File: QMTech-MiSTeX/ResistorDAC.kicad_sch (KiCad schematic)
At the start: 6 parts

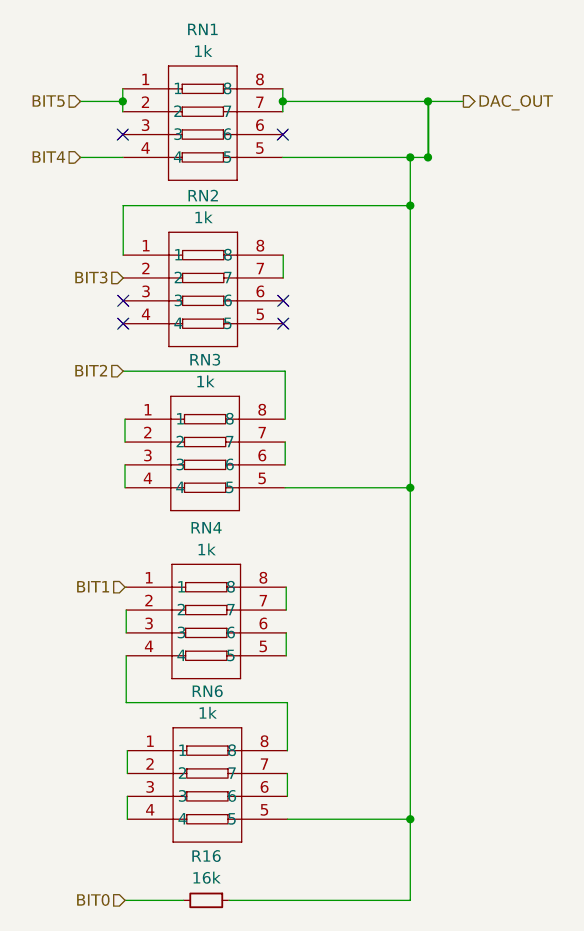
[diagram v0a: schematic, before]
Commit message: apply review notes from somhi, move audio into its own subsheet, add analog audio out
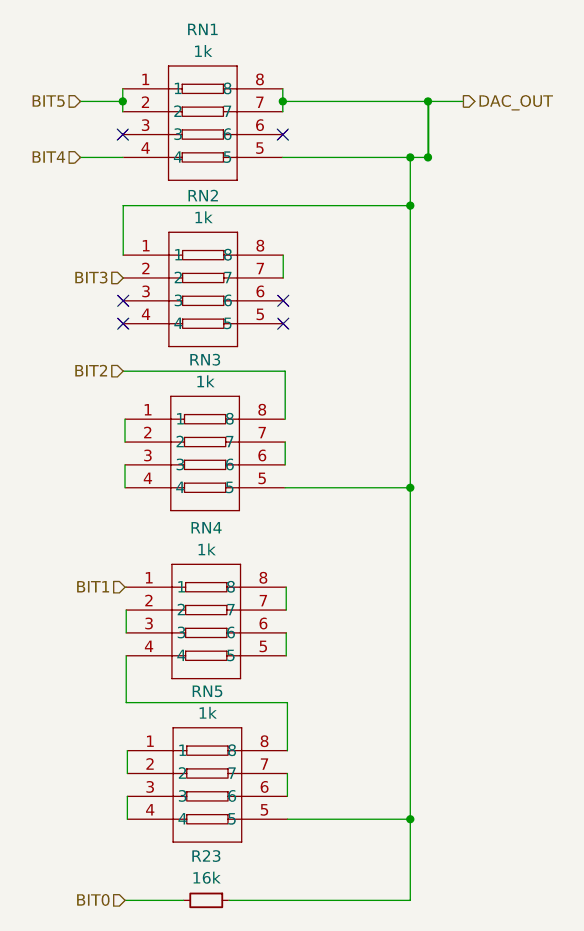
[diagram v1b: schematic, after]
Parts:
- renumbered R16 to R23, RN6 to RN5
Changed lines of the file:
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@@
         )
         (path "/bf95850e-2fcb-4784-a603-f17fc357556b/8c1d97fc-c85e-4afc-840e-7429a199eff3/cbe700d5-28fb-44ad-a669-c9e6c7dd5ddf"
-          (reference "RN1") (unit 1)
+          (reference "RN6") (unit 1)
         )
         (path "/bf95850e-2fcb-4784-a603-f17fc357556b/8c1d97fc-c85e-4afc-840e-7429a199eff3/5343cc42-a3e0-4d70-bd9b-00dc43ec6d46"
-          (reference "RN1") (unit 1)
+          (reference "RN11") (unit 1)
         )
       )
@@
   (symbol (lib_id "jlcpcb-basic-resistor-0603:16k") (at 96.393 134.747 270) (unit 1)
     (in_bom yes) (on_board yes) (dnp no) (fields_autoplaced)
-    (property "Reference" "R16" (at 96.393 129.8661 90)
+    (property "Reference" "R23" (at 96.393 129.8661 90)
       (effects (font (size 1.27 1.27)))
     )
@@
       (project "QMTech-MiSTeX"
         (path "/bf95850e-2fcb-4784-a603-f17fc357556b/8c1d97fc-c85e-4afc-840e-7429a199eff3/0f313b2c-44f6-4c87-90b4-abbb81c512aa"
-          (reference "R16") (unit 1)
+          (reference "R23") (unit 1)
         )
         (path "/bf95850e-2fcb-4784-a603-f17fc357556b/8c1d97fc-c85e-4afc-840e-7429a199eff3/cbe700d5-28fb-44ad-a669-c9e6c7dd5ddf"
-          (reference "R16") (unit 1)
+          (reference "R24") (unit 1)
         )
         (path "/bf95850e-2fcb-4784-a603-f17fc357556b/8c1d97fc-c85e-4afc-840e-7429a199eff3/5343cc42-a3e0-4d70-bd9b-00dc43ec6d46"
-          (reference "R16") (unit 1)
+          (reference "R25") (unit 1)
         )
       )
@@
         )
         (path "/bf95850e-2fcb-4784-a603-f17fc357556b/8c1d97fc-c85e-4afc-840e-7429a199eff3/cbe700d5-28fb-44ad-a669-c9e6c7dd5ddf"
-          (reference "RN2") (unit 1)
+          (reference "RN7") (unit 1)
         )
         (path "/bf95850e-2fcb-4784-a603-f17fc357556b/8c1d97fc-c85e-4afc-840e-7429a199eff3/5343cc42-a3e0-4d70-bd9b-00dc43ec6d46"
-          (reference "RN2") (unit 1)
+          (reference "RN12") (unit 1)
         )
       )
@@
         )
         (path "/bf95850e-2fcb-4784-a603-f17fc357556b/8c1d97fc-c85e-4afc-840e-7429a199eff3/cbe700d5-28fb-44ad-a669-c9e6c7dd5ddf"
-          (reference "RN4") (unit 1)
+          (reference "RN9") (unit 1)
         )
         (path "/bf95850e-2fcb-4784-a603-f17fc357556b/8c1d97fc-c85e-4afc-840e-7429a199eff3/5343cc42-a3e0-4d70-bd9b-00dc43ec6d46"
-          (reference "RN4") (unit 1)
+          (reference "RN14") (unit 1)
         )
       )
@@
   (symbol (lib_id "easyeda2kicad:4D03WGJ0102T5E") (at 96.52 121.92 0) (unit 1)
     (in_bom yes) (on_board yes) (dnp no) (fields_autoplaced)
-    (property "Reference" "RN6" (at 96.52 111.5527 0)
+    (property "Reference" "RN5" (at 96.52 111.5527 0)
       (effects (font (size 1.27 1.27)))
     )
@@
       (project "QMTech-MiSTeX"
         (path "/bf95850e-2fcb-4784-a603-f17fc357556b/8c1d97fc-c85e-4afc-840e-7429a199eff3/0f313b2c-44f6-4c87-90b4-abbb81c512aa"
-          (reference "RN6") (unit 1)
+          (reference "RN5") (unit 1)
         )
         (path "/bf95850e-2fcb-4784-a603-f17fc357556b/8c1d97fc-c85e-4afc-840e-7429a199eff3/cbe700d5-28fb-44ad-a669-c9e6c7dd5ddf"
-          (reference "RN6") (unit 1)
+          (reference "RN10") (unit 1)
         )
         (path "/bf95850e-2fcb-4784-a603-f17fc357556b/8c1d97fc-c85e-4afc-840e-7429a199eff3/5343cc42-a3e0-4d70-bd9b-00dc43ec6d46"
-          (reference "RN6") (unit 1)
+          (reference "RN15") (unit 1)
         )
       )
@@
         )
         (path "/bf95850e-2fcb-4784-a603-f17fc357556b/8c1d97fc-c85e-4afc-840e-7429a199eff3/cbe700d5-28fb-44ad-a669-c9e6c7dd5ddf"
-          (reference "RN3") (unit 1)
+          (reference "RN8") (unit 1)
         )
         (path "/bf95850e-2fcb-4784-a603-f17fc357556b/8c1d97fc-c85e-4afc-840e-7429a199eff3/5343cc42-a3e0-4d70-bd9b-00dc43ec6d46"
-          (reference "RN3") (unit 1)
+          (reference "RN13") (unit 1)
         )
       )

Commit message: finish routing/layouting, fix silk screen, add mounting holes
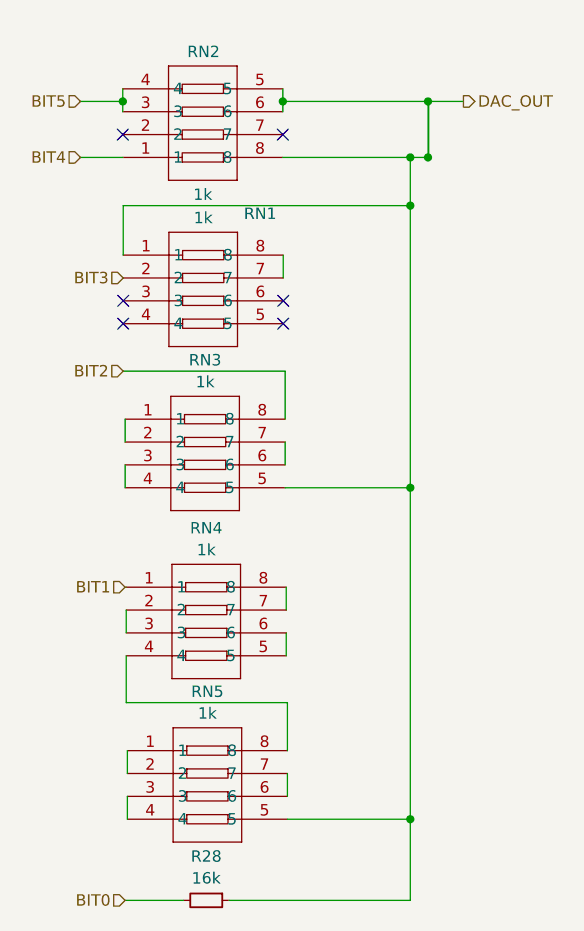
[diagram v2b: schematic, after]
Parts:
- renumbered R23 to R28
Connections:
- net BIT4: now also RN1.1; no longer RN1.4
- net BIT5: now also RN1.3, RN1.4; no longer RN1.1, RN1.2
- net DAC_OUT: now also RN1.6; no longer RN1.7
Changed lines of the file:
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@@
     (effects (font (size 1.27 1.27)) (justify right))
   )
-  (symbol (lib_id "easyeda2kicad:4D03WGJ0102T5E") (at 96.012 48.387 0) (unit 1)
-    (in_bom yes) (on_board yes) (dnp no) (fields_autoplaced)
-    (property "Reference" "RN1" (at 96.012 38.0197 0)
+  (symbol (lib_id "easyeda2kicad:4D03WGJ0102T5E") (at 96.012 48.387 0) (mirror x) (unit 1)
+    (in_bom yes) (on_board yes) (dnp no)
+    (property "Reference" "RN1" (at 102.3874 58.4454 0)
       (effects (font (size 1.27 1.27)))
     )
-    (property "Value" "1k" (at 96.012 40.4439 0)
+    (property "Value" "1k" (at 96.012 56.3301 0)
       (effects (font (size 1.27 1.27)))
     )
-    (property "Footprint" "easyeda2kicad:RES-ARRAY-SMD_0603-8P-L3.2-W1.6-BL" (at 96.012 59.817 0)
+    (property "Footprint" "easyeda2kicad:RES-ARRAY-SMD_0603-8P-L3.2-W1.6-BL" (at 96.012 36.957 0)
       (effects (font (size 1.27 1.27)) hide)
     )
-    (property "Datasheet" "https://lcsc.com/product-detail/Resistor-Networks-Arrays_1KR-102-5_C20197.html" (at 96.012 62.357 0)
+    (property "Datasheet" "https://lcsc.com/product-detail/Resistor-Networks-Arrays_1KR-102-5_C20197.html" (at 96.012 34.417 0)
       (effects (font (size 1.27 1.27)) hide)
     )
-    (property "LCSC Part" "C20197" (at 96.012 64.897 0)
+    (property "LCSC Part" "C20197" (at 96.012 31.877 0)
       (effects (font (size 1.27 1.27)) hide)
     )
@@
   (symbol (lib_id "jlcpcb-basic-resistor-0603:16k") (at 96.393 134.747 270) (unit 1)
     (in_bom yes) (on_board yes) (dnp no) (fields_autoplaced)
-    (property "Reference" "R23" (at 96.393 129.8661 90)
+    (property "Reference" "R28" (at 96.393 129.8661 90)
       (effects (font (size 1.27 1.27)))
     )
@@
       (project "QMTech-MiSTeX"
         (path "/bf95850e-2fcb-4784-a603-f17fc357556b/8c1d97fc-c85e-4afc-840e-7429a199eff3/0f313b2c-44f6-4c87-90b4-abbb81c512aa"
-          (reference "R23") (unit 1)
+          (reference "R28") (unit 1)
         )
         (path "/bf95850e-2fcb-4784-a603-f17fc357556b/8c1d97fc-c85e-4afc-840e-7429a199eff3/cbe700d5-28fb-44ad-a669-c9e6c7dd5ddf"
-          (reference "R24") (unit 1)
+          (reference "R29") (unit 1)
         )
         (path "/bf95850e-2fcb-4784-a603-f17fc357556b/8c1d97fc-c85e-4afc-840e-7429a199eff3/5343cc42-a3e0-4d70-bd9b-00dc43ec6d46"
-          (reference "R25") (unit 1)
+          (reference "R30") (unit 1)
         )
       )
@@
   )
   (symbol (lib_id "easyeda2kicad:4D03WGJ0102T5E") (at 96.0561 66.862 0) (unit 1)
-    (in_bom yes) (on_board yes) (dnp no) (fields_autoplaced)
-    (property "Reference" "RN2" (at 96.0561 56.4947 0)
+    (in_bom yes) (on_board yes) (dnp no)
+    (property "Reference" "RN2" (at 96.0882 40.4622 0)
       (effects (font (size 1.27 1.27)))
     )
@@
     )
   )
-  (symbol (lib_id "easyeda2kicad:4D03WGJ0102T5E") (at 96.393 103.759 0) (unit 1)
+  (symbol (lib_name "4D03WGJ0102T5E_2") (lib_id "easyeda2kicad:4D03WGJ0102T5E") (at 96.393 103.759 0) (unit 1)
     (in_bom yes) (on_board yes) (dnp no) (fields_autoplaced)
     (property "Reference" "RN4" (at 96.393 93.3917 0)
@@
     )
   )
-  (symbol (lib_id "easyeda2kicad:4D03WGJ0102T5E") (at 96.52 121.92 0) (unit 1)
+  (symbol (lib_name "4D03WGJ0102T5E_1") (lib_id "easyeda2kicad:4D03WGJ0102T5E") (at 96.52 121.92 0) (unit 1)
     (in_bom yes) (on_board yes) (dnp no) (fields_autoplaced)
     (property "Reference" "RN5" (at 96.52 111.5527 0)

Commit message: silkscreen, schematic titles
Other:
- title: (none) -> Weighted Resistor DAC
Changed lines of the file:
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@@
 (kicad_sch (version 20230121) (generator eeschema)
   (paper "A4")
+  (title_block
+    (title "Weighted Resistor DAC")
+  )
   (junction (at 119.0655 88.9) (diameter 0) (color 0 0 0 0)
   )
